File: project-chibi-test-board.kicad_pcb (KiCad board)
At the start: 4 copper layers, 104.1 x 134.6 mm, 221 parts, among them J1 Conn_01x04, J10 Conn_01x02, J11 Conn_01x02, J12 Conn_02x06_Top_Bottom, J13 Conn_02x06_Top_Bottom, J14 Conn_02x06_Top_Bottom, J15 Conn_02x06_Top_Bottom, J16 Conn_01x02, J17 Conn_01x02, J18 Conn_Coaxial, J19 Conn_Coaxial, J2 Conn_Coaxial, J20 Conn_01x03, J21 Conn_01x03, J22 Conn_01x04, J23 USB_B_Micro, J24 Conn_01x06, J25 Conn_01x04, J26 Conn_Coaxial, J27 Conn_Coaxial, J28 Conn_01x03, J29 Conn_01x03, J3 Conn_Coaxial, J30 Conn_01x02, J31 Conn_01x02, J32 Conn_02x06_Top_Bottom, J33 Conn_02x06_Top_Bottom, J34 Conn_02x06_Top_Bottom, J35 Conn_02x06_Top_Bottom, J36 Conn_02x06_Top_Bottom, J37 Conn_02x06_Top_Bottom, J38 Conn_02x06_Top_Bottom, J39 Conn_02x06_Top_Bottom, J4 Conn_01x03, J40 Conn_01x02, J41 Conn_01x02, J42 Conn_Coaxial, J43 Conn_Coaxial, J44 Conn_01x04, J45 Conn_01x03, J46 Conn_01x03, J47 Conn_01x06, J5 Conn_01x03, J6 Conn_02x06_Top_Bottom, J7 Conn_02x06_Top_Bottom, J8 Conn_02x06_Top_Bottom, J9 Conn_01x06, SW1 SW_DIP_x08, SW2 SW_DIP_x08, U1 40 MHz, U10 5M240ZT144C5N, U11 5M1270ZF256C5N, U2 2.048 MHz, U3 5M40ZE64C5N, U4 5M2210ZF256C5N, U5 93LC56BT-OT, U6 5M240ZT144C5N, U7 LM1117-3.3, U8 LM1117-1.8, U9 FT232H, Y1 12 MHz

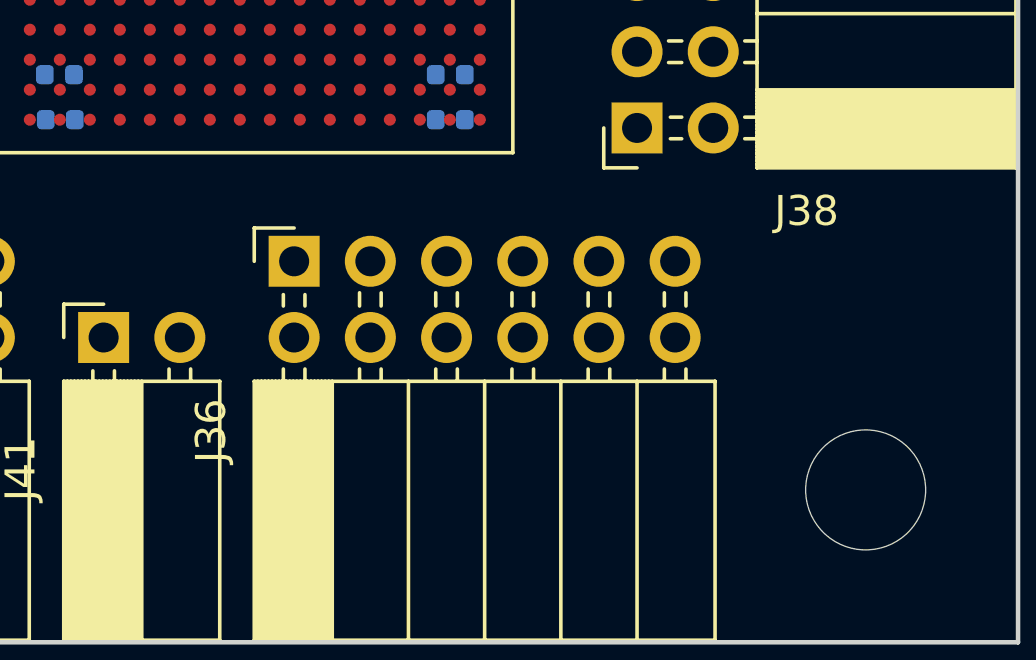
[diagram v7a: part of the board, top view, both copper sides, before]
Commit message: clean up 1270z pin ordering
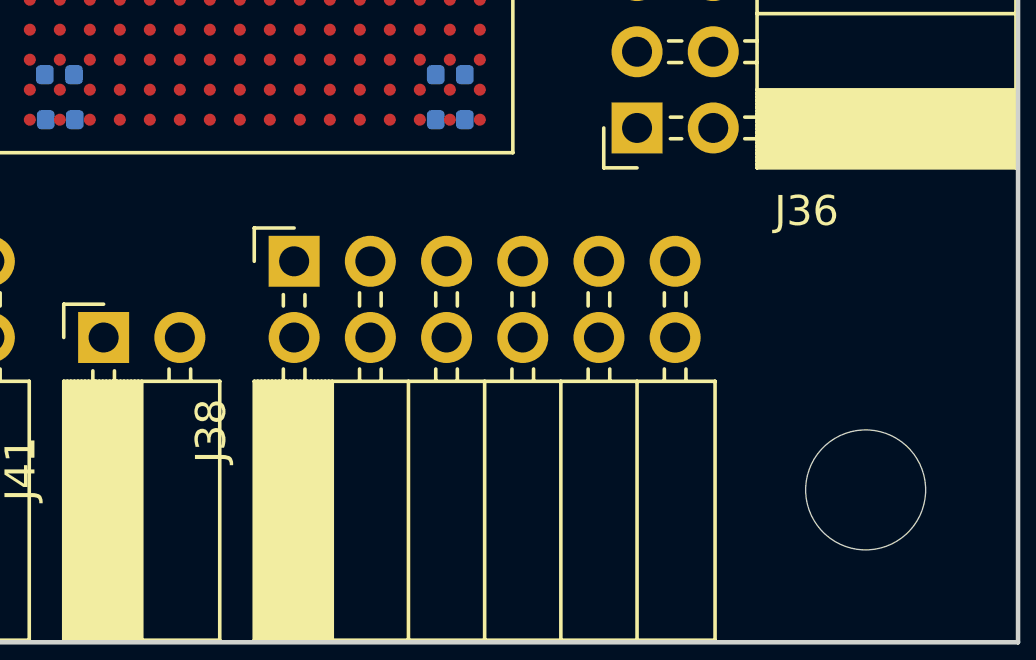
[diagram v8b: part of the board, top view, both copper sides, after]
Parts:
- moved J36 12.3 mm to (142.2, 168.3), turned to 180 degrees
- moved J38 12.3 mm to (130.8, 172.7), turned to 90 degrees
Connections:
- J36 pad 10: /tgt-10x16/EXPAND0_2 -> /tgt-10x16/EXPAND0_1
- J36 pad 11: /tgt-10x16/EXPAND0_1 -> /tgt-10x16/EXPAND0_4
- J36 pad 2: GND -> +3V3
- J36 pad 3: /tgt-10x16/EXPAND0_7 -> GND
- J36 pad 4: /tgt-10x16/EXPAND0_6 -> GND
- J36 pad 5: /tgt-10x16/EXPAND0_5 -> /tgt-10x16/EXPAND0_7
- J36 pad 6: /tgt-10x16/EXPAND0_4 -> /tgt-10x16/EXPAND0_3
- J36 pad 7: +3V3 -> /tgt-10x16/EXPAND0_6
- J36 pad 8: GND -> /tgt-10x16/EXPAND0_2
- J36 pad 9: /tgt-10x16/EXPAND0_3 -> /tgt-10x16/EXPAND0_5
- J37 pad 10: /tgt-10x16/EXPAND1_2 -> /tgt-10x16/EXPAND1_1
- J37 pad 11: /tgt-10x16/EXPAND1_1 -> /tgt-10x16/EXPAND1_4
- J37 pad 2: GND -> +3V3
- J37 pad 3: /tgt-10x16/EXPAND1_7 -> GND
- J37 pad 4: /tgt-10x16/EXPAND1_6 -> GND
- J37 pad 5: /tgt-10x16/EXPAND1_5 -> /tgt-10x16/EXPAND1_7
- J37 pad 6: /tgt-10x16/EXPAND1_4 -> /tgt-10x16/EXPAND1_3
- J37 pad 7: +3V3 -> /tgt-10x16/EXPAND1_6
- J37 pad 8: GND -> /tgt-10x16/EXPAND1_2
- J37 pad 9: /tgt-10x16/EXPAND1_3 -> /tgt-10x16/EXPAND1_5
- J38 pad 10: /tgt-10x16/EXPAND2_2 -> /tgt-10x16/EXPAND2_1
- J38 pad 11: /tgt-10x16/EXPAND2_1 -> /tgt-10x16/EXPAND2_4
- J38 pad 2: GND -> +3V3
- J38 pad 3: /tgt-10x16/EXPAND2_7 -> GND
- J38 pad 4: /tgt-10x16/EXPAND2_6 -> GND
- J38 pad 5: /tgt-10x16/EXPAND2_5 -> /tgt-10x16/EXPAND2_7
- J38 pad 6: /tgt-10x16/EXPAND2_4 -> /tgt-10x16/EXPAND2_3
- J38 pad 7: +3V3 -> /tgt-10x16/EXPAND2_6
- J38 pad 8: GND -> /tgt-10x16/EXPAND2_2
- J38 pad 9: /tgt-10x16/EXPAND2_3 -> /tgt-10x16/EXPAND2_5
- J39 pad 10: /tgt-10x16/EXPAND3_2 -> /tgt-10x16/EXPAND3_1
- J39 pad 11: /tgt-10x16/EXPAND3_1 -> /tgt-10x16/EXPAND3_4
- J39 pad 2: GND -> +3V3
- J39 pad 3: /tgt-10x16/EXPAND3_7 -> GND
- J39 pad 4: /tgt-10x16/EXPAND3_6 -> GND
- J39 pad 5: /tgt-10x16/EXPAND3_5 -> /tgt-10x16/EXPAND3_7
- J39 pad 6: /tgt-10x16/EXPAND3_4 -> /tgt-10x16/EXPAND3_3
- J39 pad 7: +3V3 -> /tgt-10x16/EXPAND3_6
- J39 pad 8: GND -> /tgt-10x16/EXPAND3_2
- J39 pad 9: /tgt-10x16/EXPAND3_3 -> /tgt-10x16/EXPAND3_5
